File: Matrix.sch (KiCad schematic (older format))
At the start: 173 parts

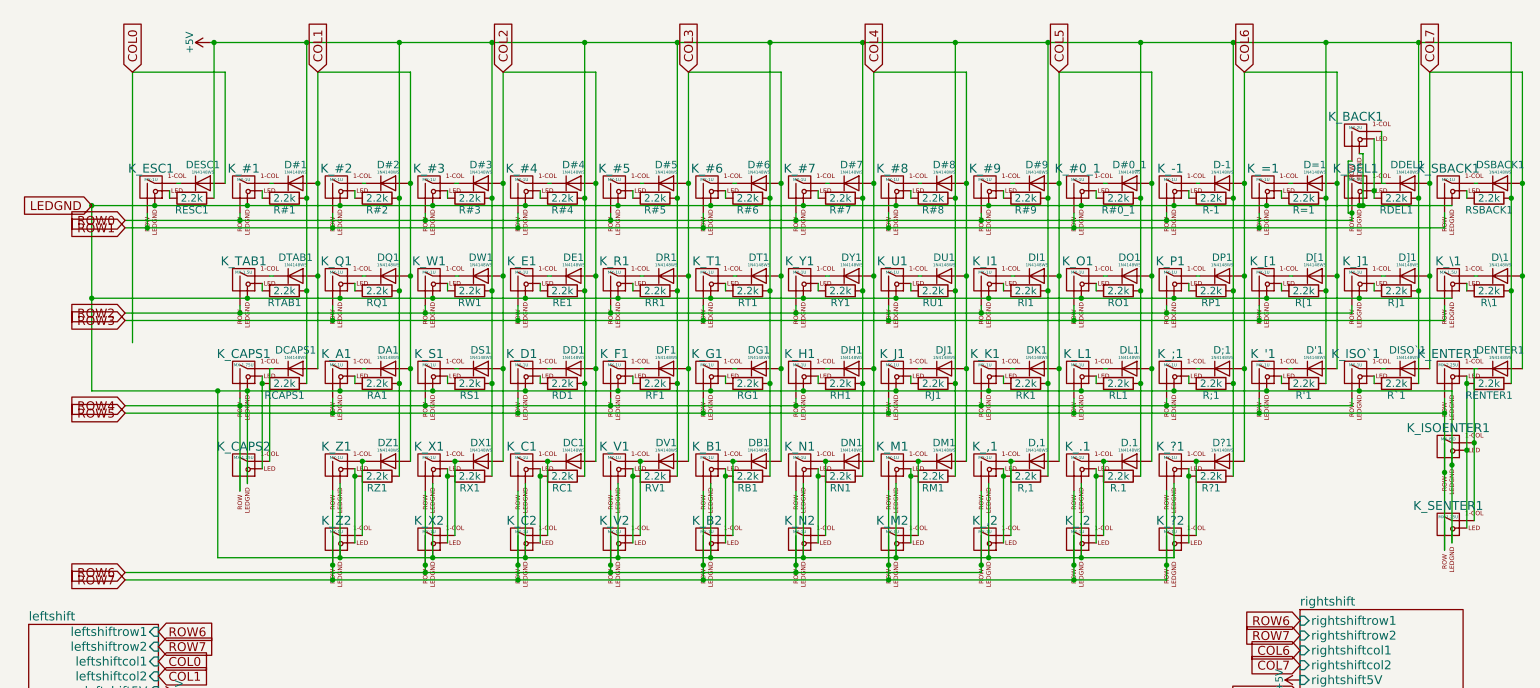
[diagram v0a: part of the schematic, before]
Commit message: Begin rework of schematic
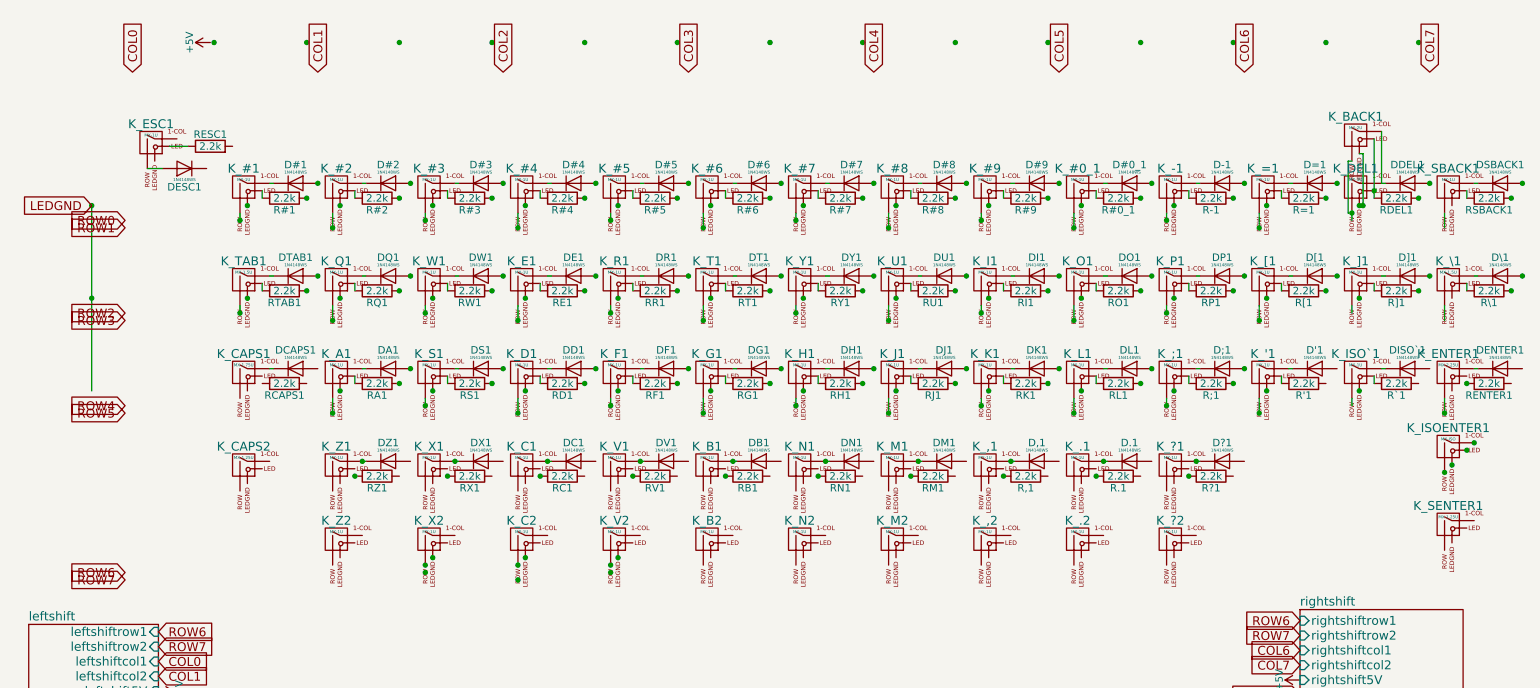
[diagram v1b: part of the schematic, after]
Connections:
- wire segments 243 -> 142
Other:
- moved on the sheet: DESC1, K_ESC1, RESC1

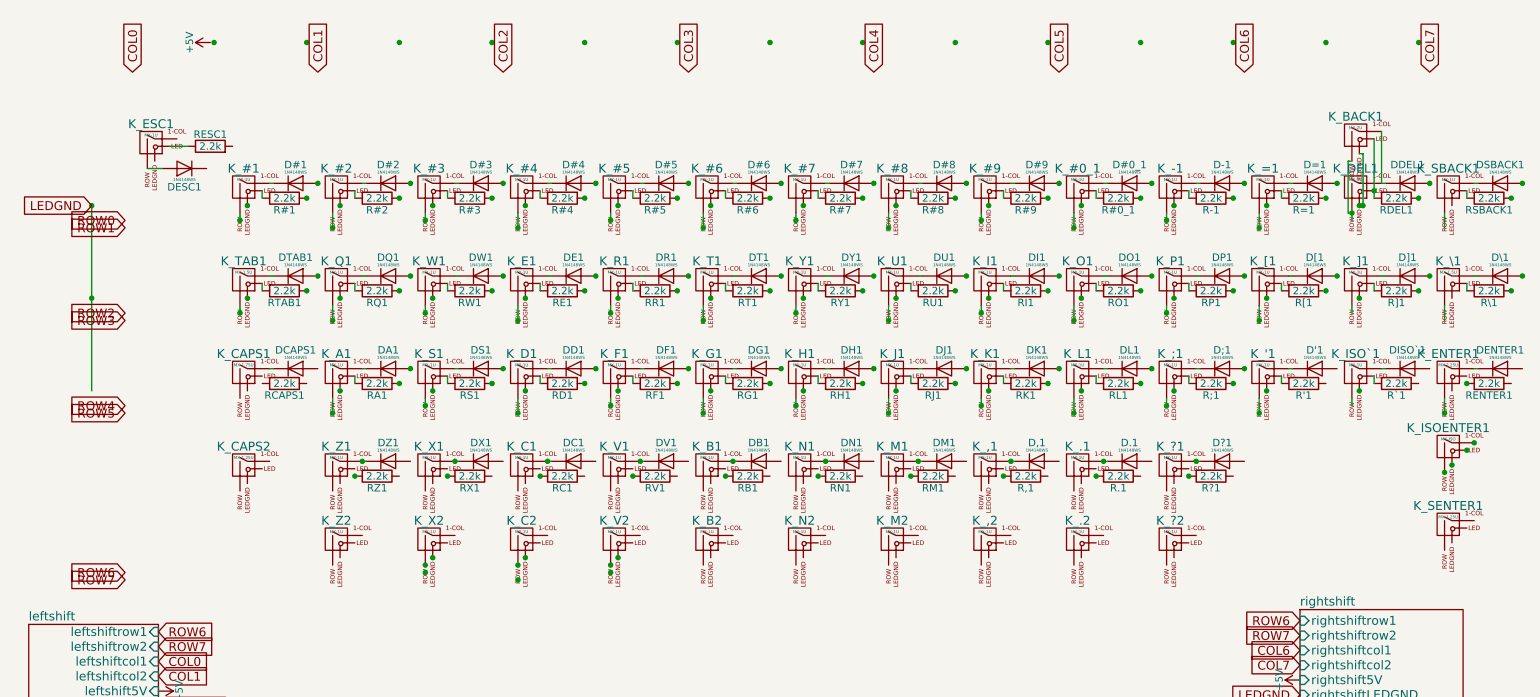
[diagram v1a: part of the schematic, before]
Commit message: Erase the schematic main grid
Clean slate
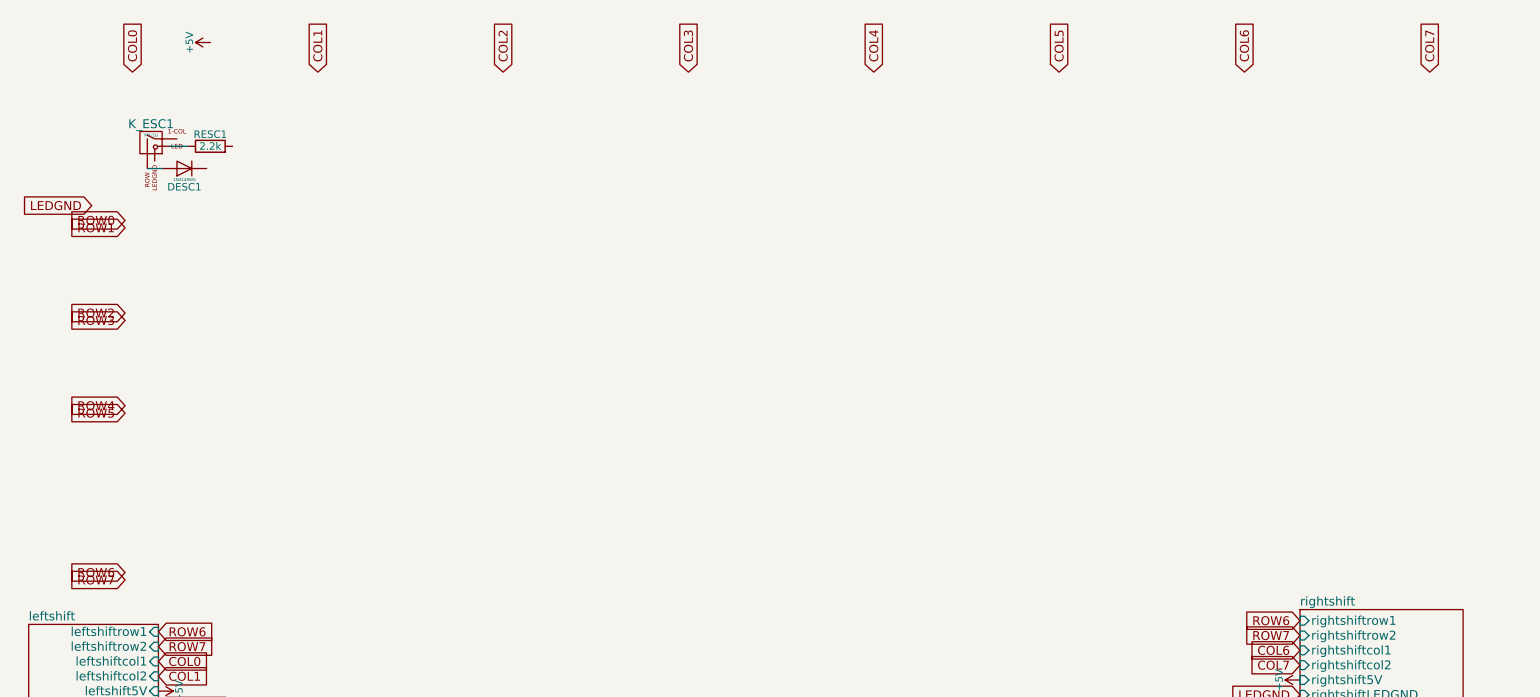
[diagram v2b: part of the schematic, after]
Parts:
- removed D#0_1, D#1, D#2, D#3, D#4, D#5, D#6, D#7, D#8, D#9, D'1, D,1, D-1, D.1, D;1, D=1, D?1, DA1, DB1, DC1, DCAPS1, DD1, DDEL1, DE1, DENTER1, DF1, DG1, DH1, DI1, DISO`1, DJ1, DK1, DL1, DM1, DN1, DO1, DP1, DQ1, DR1, DS1, DSBACK1, DT1, DTAB1, DU1, DV1, DW1, DX1, DY1, DZ1, D[1, D\1, D]1: 1N4148WS, symbol D
- removed K_#0_1, K_#1, K_#2, K_#3, K_#4, K_#5, K_#6, K_#7, K_#8, K_#9, K_'1, K_,1, K_,2, K_-1, K_.1, K_.2, K_;1, K_=1, K_?1, K_?2, K_A1, K_B1, K_B2, K_C1, K_C2, K_D1, K_DEL1, K_E1, K_F1, K_G1, K_H1, K_I1, K_ISO`1, K_J1, K_K1, K_L1, K_M1, K_M2, K_N1, K_N2, K_O1, K_P1, K_Q1, K_R1, K_S1, K_SBACK1, K_T1, K_U1, K_V1, K_V2, K_W1, K_X1, K_X2, K_Y1, K_Z1, K_Z2, K_[1, K_]1: MX-1U, MX_Alps_Hybrid:MX-1U, symbol MX-1U
- removed K_BACK1: MX-2U, MX_Alps_Hybrid:MX-2U, symbol MX-2U
- removed K_CAPS1: MX-1.75U, MX_Alps_Hybrid:MX-1.75U, symbol MX-1.75U
- removed K_CAPS2, K_SENTER1: MX-1.25U, MX_Alps_Hybrid:MX-1.25U, symbol MX-1.25U
- removed K_ENTER1: MX-2.25U, MX_Alps_Hybrid:MX-2.25U, symbol MX-2.25U
- removed K_ISOENTER1: MX-ISO, MX_Alps_Hybrid:MX-ISO-Combined, symbol MX-ISO
- removed K_TAB1, K_\1: MX-1.5U, MX_Alps_Hybrid:MX-1.5U, symbol MX-1.5U
- removed R#0_1, R#1, R#2, R#3, R#4, R#5, R#6, R#7, R#8, R#9, R'1, R,1, R-1, R.1, R;1, R=1, R?1, RA1, RB1, RC1, RCAPS1, RD1, RDEL1, RE1, RENTER1, RF1, RG1, RH1, RI1, RJ1, RK1, RL1, RM1, RN1, RO1, RP1, RQ1, RR1, RS1, RSBACK1, RT1, RTAB1, RU1, RV1, RW1, RX1, RY1, RZ1, R[1, R\1, R]1, R`1: 2.2k, symbol R
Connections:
- wire segments 142 -> 2

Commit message: Clone a bunch of keys
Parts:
- added DESC? (x56): 1N4148WS, symbol D
- added K_ESC? (x56): MX-1U, MX_Alps_Hybrid:MX-1U, symbol MX-1U
- added RESC? (x56): 2.2k, symbol R
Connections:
- new net: DESC?.2 (A), K_ESC?.2 (ROW) (x56)
- new net: K_ESC?.3 (LED), RESC?.1 (x56)
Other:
- moved on the sheet: DESC1, K_ESC1, RESC1

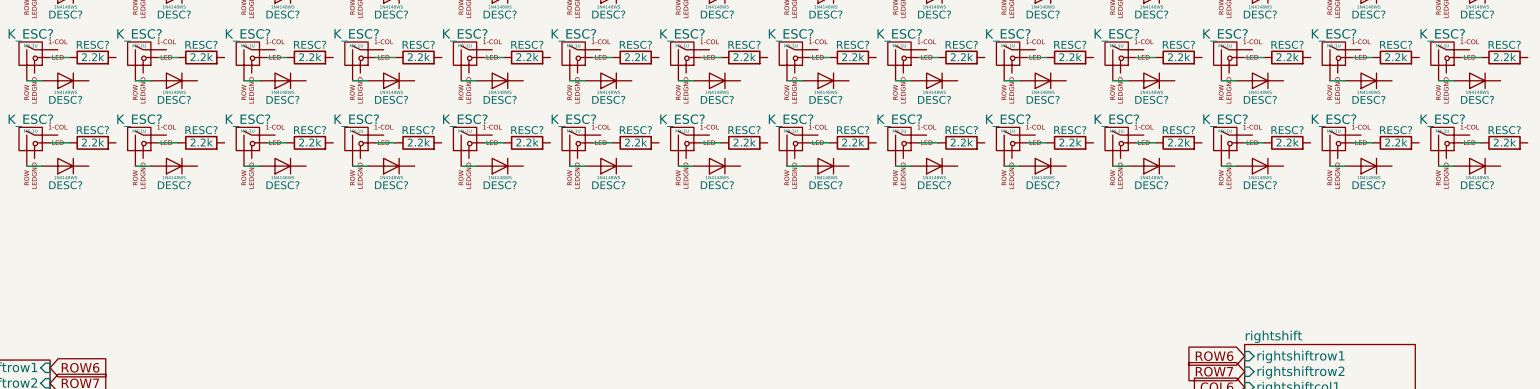
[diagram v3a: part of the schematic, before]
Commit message: Rebuild key placement, unwired
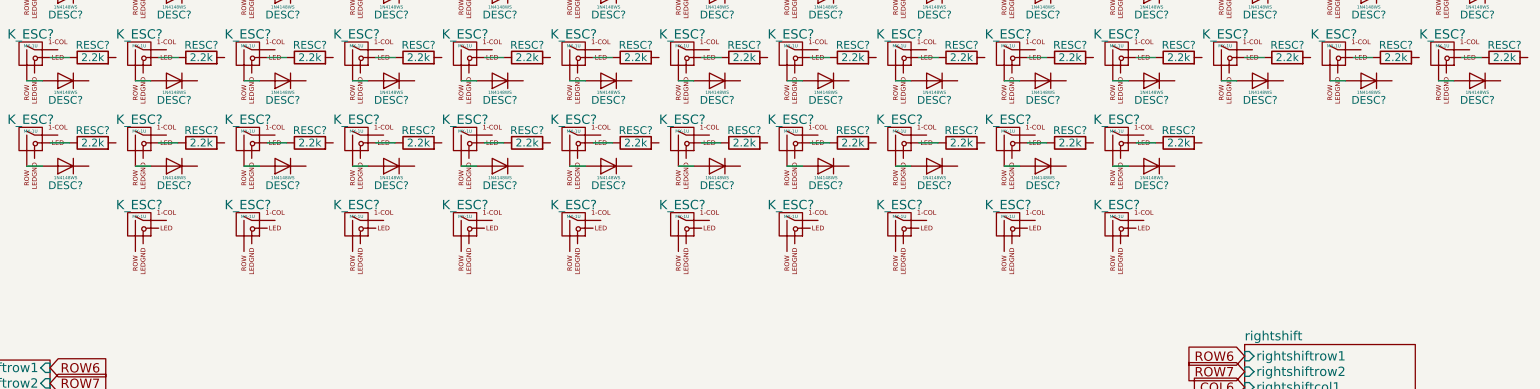
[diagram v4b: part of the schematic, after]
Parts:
- removed DESC? (x3): 1N4148WS, symbol D
- removed K_ESC? (x3): MX-1U, MX_Alps_Hybrid:MX-1U, symbol MX-1U
- removed RESC? (x3): 2.2k, symbol R
- added K_ESC? (x10): MX-1U, MX_Alps_Hybrid:MX-1U, symbol MX-1U
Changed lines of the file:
@@
 $Comp
 L MX-1U K_ESC?
-U 1 1 597E5E99
-P 9200 3175
-F 0 "K_ESC?" H 9200 3300 60  0000 C CNN
-F 1 "MX-1U" H 9200 3225 20  0000 C CNN
-F 2 "MX_Alps_Hybrid:MX-1U" H 9175 3150 60  0001 C CNN
-F 3 "" H 9175 3150 60  0001 C CNN
-	1    9200 3175
+U 1 1 597EB000
+P 2200 3725
+F 0 "K_ESC?" H 2200 3850 60  0000 C CNN
+F 1 "MX-1U" H 2200 3775 20  0000 C CNN
+F 2 "MX_Alps_Hybrid:MX-1U" H 2175 3700 60  0001 C CNN
+F 3 "" H 2175 3700 60  0001 C CNN
+	1    2200 3725
 	1    0    0    -1
 $EndComp
 $Comp
-L R RESC?
-U 1 1 597E5E9F
-P 9600 3200
-F 0 "RESC?" V 9680 3200 50  0000 C CNN
-F 1 "2.2k" V 9600 3200 50  0000 C CNN
-F 2 "" V 9530 3200 50  0001 C CNN
-F 3 "" H 9600 3200 50  0001 C CNN
-	1    9600 3200
-	0    -1   -1   0
-$EndComp
-$Comp
-L D DESC?
-U 1 1 597E5EA5
-P 9425 3350
-F 0 "DESC?" H 9425 3475 50  0000 C CNN
-F 1 "1N4148WS" H 9425 3425 20  0000 C CNN
-F 2 "" H 9425 3350 50  0001 C CNN
-F 3 "" H 9425 3350 50  0001 C CNN
-	1    9425 3350
-	-1   0    0    1
-$EndComp
-Wire Wire Line
-	9450 3200 9325 3200
-Wire Wire Line
-	9175 3350 9275 3350
-$Comp
 L MX-1U K_ESC?
-U 1 1 597E5EAD
-P 9900 3175
-F 0 "K_ESC?" H 9900 3300 60  0000 C CNN
-F 1 "MX-1U" H 9900 3225 20  0000 C CNN
-F 2 "MX_Alps_Hybrid:MX-1U" H 9875 3150 60  0001 C CNN
-F 3 "" H 9875 3150 60  0001 C CNN
-	1    9900 3175
+U 1 1 597EB014
+P 2900 3725
+F 0 "K_ESC?" H 2900 3850 60  0000 C CNN
+F 1 "MX-1U" H 2900 3775 20  0000 C CNN
+F 2 "MX_Alps_Hybrid:MX-1U" H 2875 3700 60  0001 C CNN
+F 3 "" H 2875 3700 60  0001 C CNN
+	1    2900 3725
 	1    0    0    -1
 $EndComp
 $Comp
-L R RESC?
-U 1 1 597E5EB3
-P 10300 3200
-F 0 "RESC?" V 10380 3200 50  0000 C CNN
-F 1 "2.2k" V 10300 3200 50  0000 C CNN
-F 2 "" V 10230 3200 50  0001 C CNN
-F 3 "" H 10300 3200 50  0001 C CNN
-	1    10300 3200
-	0    -1   -1   0
-$EndComp
-$Comp
-L D DESC?
-U 1 1 597E5EB9
-P 10125 3350
-F 0 "DESC?" H 10125 3475 50  0000 C CNN
-F 1 "1N4148WS" H 10125 3425 20  0000 C CNN
-F 2 "" H 10125 3350 50  0001 C CNN
-F 3 "" H 10125 3350 50  0001 C CNN
-	1    10125 3350
-	-1   0    0    1
-$EndComp
-Wire Wire Line
-	10150 3200 10025 3200
-Wire Wire Line
-	9875 3350 9975 3350
-$Comp
 L MX-1U K_ESC?
-U 1 1 597E5EC1
-P 10600 3175
-F 0 "K_ESC?" H 10600 3300 60  0000 C CNN
-F 1 "MX-1U" H 10600 3225 20  0000 C CNN
-F 2 "MX_Alps_Hybrid:MX-1U" H 10575 3150 60  0001 C CNN
-F 3 "" H 10575 3150 60  0001 C CNN
-	1    10600 3175
+U 1 1 597EB028
+P 3600 3725
+F 0 "K_ESC?" H 3600 3850 60  0000 C CNN
+F 1 "MX-1U" H 3600 3775 20  0000 C CNN
+F 2 "MX_Alps_Hybrid:MX-1U" H 3575 3700 60  0001 C CNN
+F 3 "" H 3575 3700 60  0001 C CNN
+	1    3600 3725
 	1    0    0    -1
 $EndComp
 $Comp
-L R RESC?
-U 1 1 597E5EC7
-P 11000 3200
-F 0 "RESC?" V 11080 3200 50  0000 C CNN
-F 1 "2.2k" V 11000 3200 50  0000 C CNN
-F 2 "" V 10930 3200 50  0001 C CNN
-F 3 "" H 11000 3200 50  0001 C CNN
-	1    11000 3200
-	0    -1   -1   0
+L MX-1U K_ESC?
+U 1 1 597EB03C
+P 4300 3725
+F 0 "K_ESC?" H 4300 3850 60  0000 C CNN
+F 1 "MX-1U" H 4300 3775 20  0000 C CNN
+F 2 "MX_Alps_Hybrid:MX-1U" H 4275 3700 60  0001 C CNN
+F 3 "" H 4275 3700 60  0001 C CNN
+	1    4300 3725
+	1    0    0    -1
 $EndComp
 $Comp
-L D DESC?
-U 1 1 597E5ECD
-P 10825 3350
-F 0 "DESC?" H 10825 3475 50  0000 C CNN
-F 1 "1N4148WS" H 10825 3425 20  0000 C CNN
-F 2 "" H 10825 3350 50  0001 C CNN
-F 3 "" H 10825 3350 50  0001 C CNN
-	1    10825 3350
-	-1   0    0    1
+L MX-1U K_ESC?
+U 1 1 597EB050
+P 5000 3725
+F 0 "K_ESC?" H 5000 3850 60  0000 C CNN
+F 1 "MX-1U" H 5000 3775 20  0000 C CNN
+F 2 "MX_Alps_Hybrid:MX-1U" H 4975 3700 60  0001 C CNN
+F 3 "" H 4975 3700 60  0001 C CNN
+	1    5000 3725
+	1    0    0    -1
 $EndComp
-Wire Wire Line
-	10850 3200 10725 3200
-Wire Wire Line
-	10575 3350 10675 3350
+$Comp
+L MX-1U K_ESC?
+U 1 1 597EB064
+P 5700 3725
+F 0 "K_ESC?" H 5700 3850 60  0000 C CNN
+F 1 "MX-1U" H 5700 3775 20  0000 C CNN
+F 2 "MX_Alps_Hybrid:MX-1U" H 5675 3700 60  0001 C CNN
+F 3 "" H 5675 3700 60  0001 C CNN
+	1    5700 3725
+	1    0    0    -1
+$EndComp
+$Comp
+L MX-1U K_ESC?
+U 1 1 597EB078
+P 6400 3725
+F 0 "K_ESC?" H 6400 3850 60  0000 C CNN
+F 1 "MX-1U" H 6400 3775 20  0000 C CNN
+F 2 "MX_Alps_Hybrid:MX-1U" H 6375 3700 60  0001 C CNN
+F 3 "" H 6375 3700 60  0001 C CNN
+	1    6400 3725
+	1    0    0    -1
+$EndComp
+$Comp
+L MX-1U K_ESC?
+U 1 1 597EB08C
+P 7100 3725
+F 0 "K_ESC?" H 7100 3850 60  0000 C CNN
+F 1 "MX-1U" H 7100 3775 20  0000 C CNN
+F 2 "MX_Alps_Hybrid:MX-1U" H 7075 3700 60  0001 C CNN
+F 3 "" H 7075 3700 60  0001 C CNN
+	1    7100 3725
+	1    0    0    -1
+$EndComp
+$Comp
+L MX-1U K_ESC?
+U 1 1 597EB0A0
+P 7800 3725
+F 0 "K_ESC?" H 7800 3850 60  0000 C CNN
+F 1 "MX-1U" H 7800 3775 20  0000 C CNN
+F 2 "MX_Alps_Hybrid:MX-1U" H 7775 3700 60  0001 C CNN
+F 3 "" H 7775 3700 60  0001 C CNN
+	1    7800 3725
+	1    0    0    -1
+$EndComp
+$Comp
+L MX-1U K_ESC?
+U 1 1 597EB0B4
+P 8500 3725
+F 0 "K_ESC?" H 8500 3850 60  0000 C CNN
+F 1 "MX-1U" H 8500 3775 20  0000 C CNN
+F 2 "MX_Alps_Hybrid:MX-1U" H 8475 3700 60  0001 C CNN
+F 3 "" H 8475 3700 60  0001 C CNN
+	1    8500 3725
+	1    0    0    -1
+$EndComp
 $EndSCHEMATC
